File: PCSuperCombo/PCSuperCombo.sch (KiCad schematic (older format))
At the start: 42 parts, among them CN1 DB9 Male, J1 IDE_CONNECTOR, J2 CF Adapter Power, J3 Bus_ISA_8bit, J4 LED, SW1 Options, U1 BIOS FLASH, U10 1.8432 MHz, U2 74HCT245, U3 ATF/GAL16V8x-15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

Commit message: PCSuperCombo WIP.
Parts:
- added R10, R11: 0R, Resistor_SMD:R_1206_3216Metric, symbol Device:R
- renumbered R10 to R12, R11 to R13
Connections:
- net COM1_ENABLE: now also R9.2, SW1.14, R10.1; no longer R8.2, SW1.17
- net D0: no longer U8.43 (D0)
- net D0_BUF: now also U8.43 (D0); no longer U1.13 (D0)
- net D1: no longer U8.44 (D1)
- net D1_BUF: now also U8.44 (D1); no longer U1.14 (D1)
- net D2: no longer U8.45 (D2)
- net D2_BUF: now also U8.45 (D2); no longer U1.15 (D2)
- net D3: no longer U8.46 (D3)
- net D3_BUF: now also U8.46 (D3); no longer U1.17 (D3)
- net D4: no longer U8.47 (D4)
- net D4_BUF: now also U8.47 (D4); no longer U1.18 (D4)
- net D5: no longer U8.2 (D5)
- net D5_BUF: now also U8.2 (D5); no longer U1.19 (D5)
- net D6: no longer U8.3 (D6)
- net D6_BUF: now also U8.3 (D6); no longer U1.20 (D6)
- net D7: no longer U8.4 (D7)
- net D7_BUF: now also U8.4 (D7); no longer U1.21 (D7)
- net GND: now also SW1.11, R10.2; no longer SW1.9
- net V20_JUMPER: now also R8.2, SW1.17; no longer R9.2, SW1.16
- net ~CARD_SEL: now also SW1.16; no longer SW1.13
- net ~CE~_BIOS: now also SW1.12, R11.2; no longer SW1.11
- net ~CE~_BIOS_THRU: now also SW1.13, R11.1; no longer SW1.14
- net ~IOR_OR_MEMR: now also SW1.9; no longer SW1.12
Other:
- moved on the sheet: C1, C10, C2, C3, C4, C5, C6, C7, C8, C9, R1, R2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

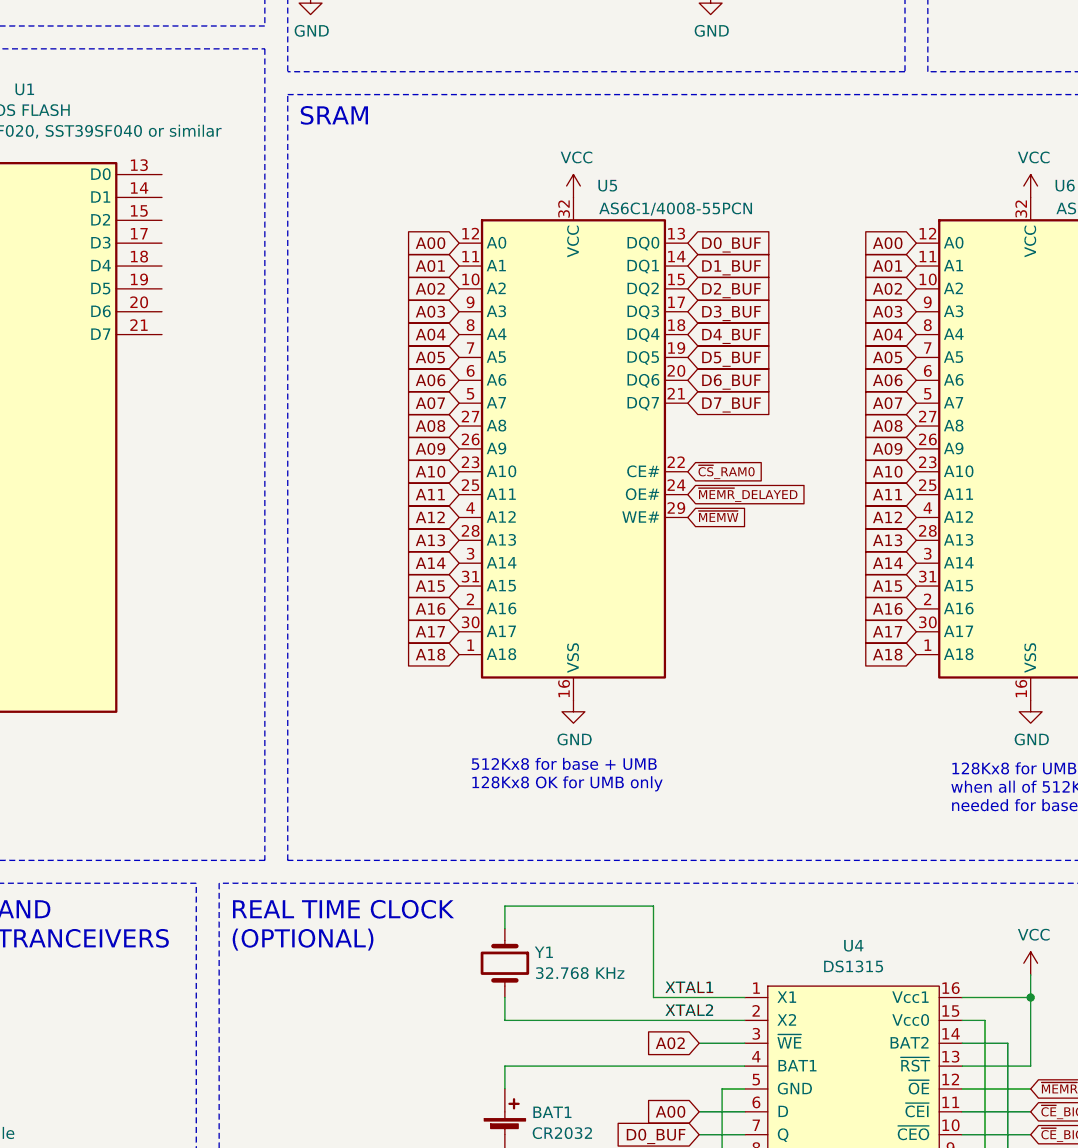
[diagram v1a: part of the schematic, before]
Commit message: Committing some old edits from mid-2022 to PCSuperCombo. Not sure if these are good changes that should be comitted.
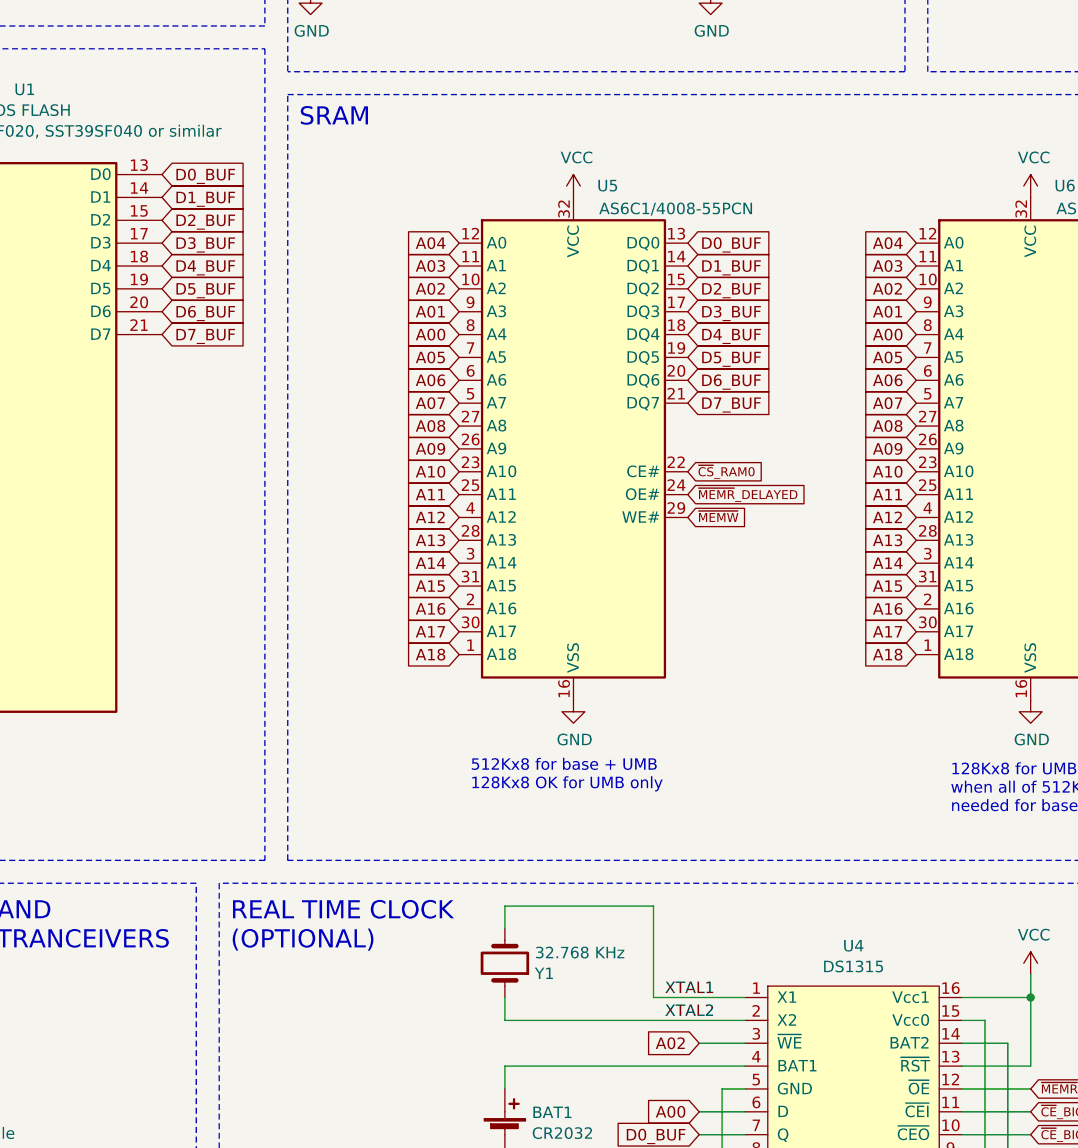
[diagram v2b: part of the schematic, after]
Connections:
- net A00: now also U5.8 (A4), U6.8 (A4); no longer U5.12 (A0), U6.12 (A0)
- net A01: now also U5.9 (A3), U6.9 (A3); no longer U5.11 (A1), U6.11 (A1)
- net A03: now also U5.11 (A1), U6.11 (A1); no longer U5.9 (A3), U6.9 (A3)
- net A04: now also U5.12 (A0), U6.12 (A0); no longer U5.8 (A4), U6.8 (A4)
- net D0_BUF: now also U1.13 (D0)
- net D1_BUF: now also U1.14 (D1)
- net D2_BUF: now also U1.15 (D2)
- net D3_BUF: now also U1.17 (D3)
- net D4_BUF: now also U1.18 (D4)
- net D5_BUF: now also U1.19 (D5)
- net D6_BUF: now also U1.20 (D6)
- net D7_BUF: now also U1.21 (D7)
- net XTAL1: now also Y1.2; no longer Y1.1
- net XTAL2: now also Y1.1; no longer Y1.2
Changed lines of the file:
@@
 F 3 "~" H 9400 7250 50  0001 C CNN
 	1    9400 7250
-	0    1    1    0
+	0    1    -1   0
 $EndComp
 Wire Wire Line
@@
 	1    0    0    -1
 $EndComp
-Text GLabel 9200 4100 0    50   Input ~ 0
-A00
-Text GLabel 9200 4200 0    50   Input ~ 0
-A01
-Text GLabel 9200 4300 0    50   Input ~ 0
-A02
-Text GLabel 9200 4400 0    50   Input ~ 0
-A03
-Text GLabel 9200 4500 0    50   Input ~ 0
-A04
 Text GLabel 9200 4600 0    50   Input ~ 0
 A05
@@
 Wire Notes Line
 	15950 3450 15950 6800
-Text GLabel 11200 4100 0    50   Input ~ 0
-A00
-Text GLabel 11200 4200 0    50   Input ~ 0
-A01
-Text GLabel 11200 4300 0    50   Input ~ 0
-A02
-Text GLabel 11200 4400 0    50   Input ~ 0
-A03
-Text GLabel 11200 4500 0    50   Input ~ 0
-A04
 Text GLabel 11200 4600 0    50   Input ~ 0
 A05
@@
 	1    0    0    -1
 $EndComp
+Text GLabel 9200 4500 0    50   Input ~ 0
+A00
+Text GLabel 9200 4400 0    50   Input ~ 0
+A01
+Text GLabel 9200 4300 0    50   Input ~ 0
+A02
+Text GLabel 9200 4200 0    50   Input ~ 0
+A03
+Text GLabel 9200 4100 0    50   Input ~ 0
+A04
+Text GLabel 11200 4500 0    50   Input ~ 0
+A00
+Text GLabel 11200 4400 0    50   Input ~ 0
+A01
+Text GLabel 11200 4300 0    50   Input ~ 0
+A02
+Text GLabel 11200 4200 0    50   Input ~ 0
+A03
+Text GLabel 11200 4100 0    50   Input ~ 0
+A04
+Text GLabel 7900 3800 2    50   Input ~ 0
+D0_BUF
+Text GLabel 7900 3900 2    50   Input ~ 0
+D1_BUF
+Text GLabel 7900 4000 2    50   Input ~ 0
+D2_BUF
+Text GLabel 7900 4100 2    50   Input ~ 0
+D3_BUF
+Text GLabel 7900 4200 2    50   Input ~ 0
+D4_BUF
+Text GLabel 7900 4300 2    50   Input ~ 0
+D5_BUF
+Text GLabel 7900 4400 2    50   Input ~ 0
+D6_BUF
+Text GLabel 7900 4500 2    50   Input ~ 0
+D7_BUF
 $EndSCHEMATC
